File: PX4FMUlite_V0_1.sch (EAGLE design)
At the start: 192 parts, among them J201 DF13C-6P-1.25V, J202 DF13C-6P-1.25V, J203 DF13C-6P-1.25V, J204 DF13C-6P-1.25V, J301 47346-0001, J302 DF13C-4P-1.25V, J401 DF13C-4P-1.25V, J403 DF13C-7P-1.25V, J404 DF13C-5P-1.25V, J405 DF13C-4P-1.25V, J601 DF13C-6P-1.25V, J702 DF13C-3P-1.25V, J801 JST-ZH-3, J901 HEADER-3X163X16RA, M3_MOUNT1101 MOUNT-HOLE3.1MM, M3_MOUNT1102 MOUNT-HOLE3.1MM, M3_MOUNT1103 MOUNT-HOLE3.1MM, M3_MOUNT1104 MOUNT-HOLE3.1MM, U101 STM32F4X7VX, U102 FM25V01, U201 TXS0108QFN20, U202 TXS0108QFN20, U301 2908-05WB-MG, U401 MAX3051, U502 L3GD20H, U503 MS5611-01BA, U701 TCA62724FMG, U703 LRTB GFTG-T7AW-1+V7A7-29+R5T9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, U901 TXS0108QFN20, U903 74LVC2G240, X101 3.2x2.5 mm / 24 MHz / 15 ppm

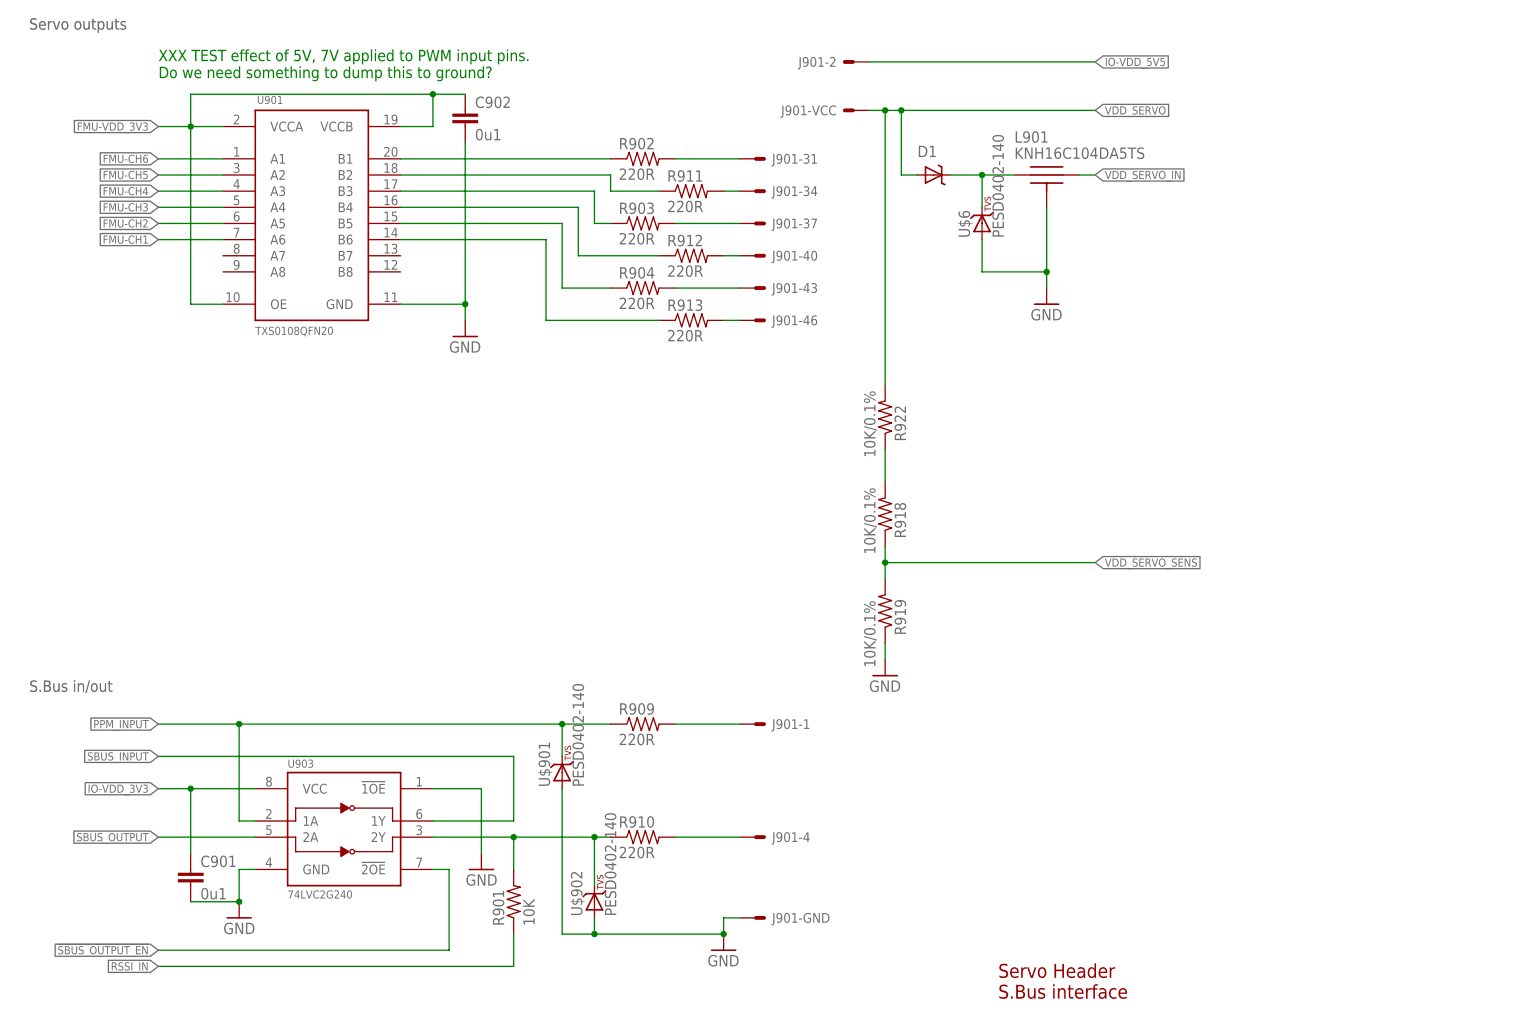
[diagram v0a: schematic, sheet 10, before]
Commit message: Resize board, resized servo conn plus more
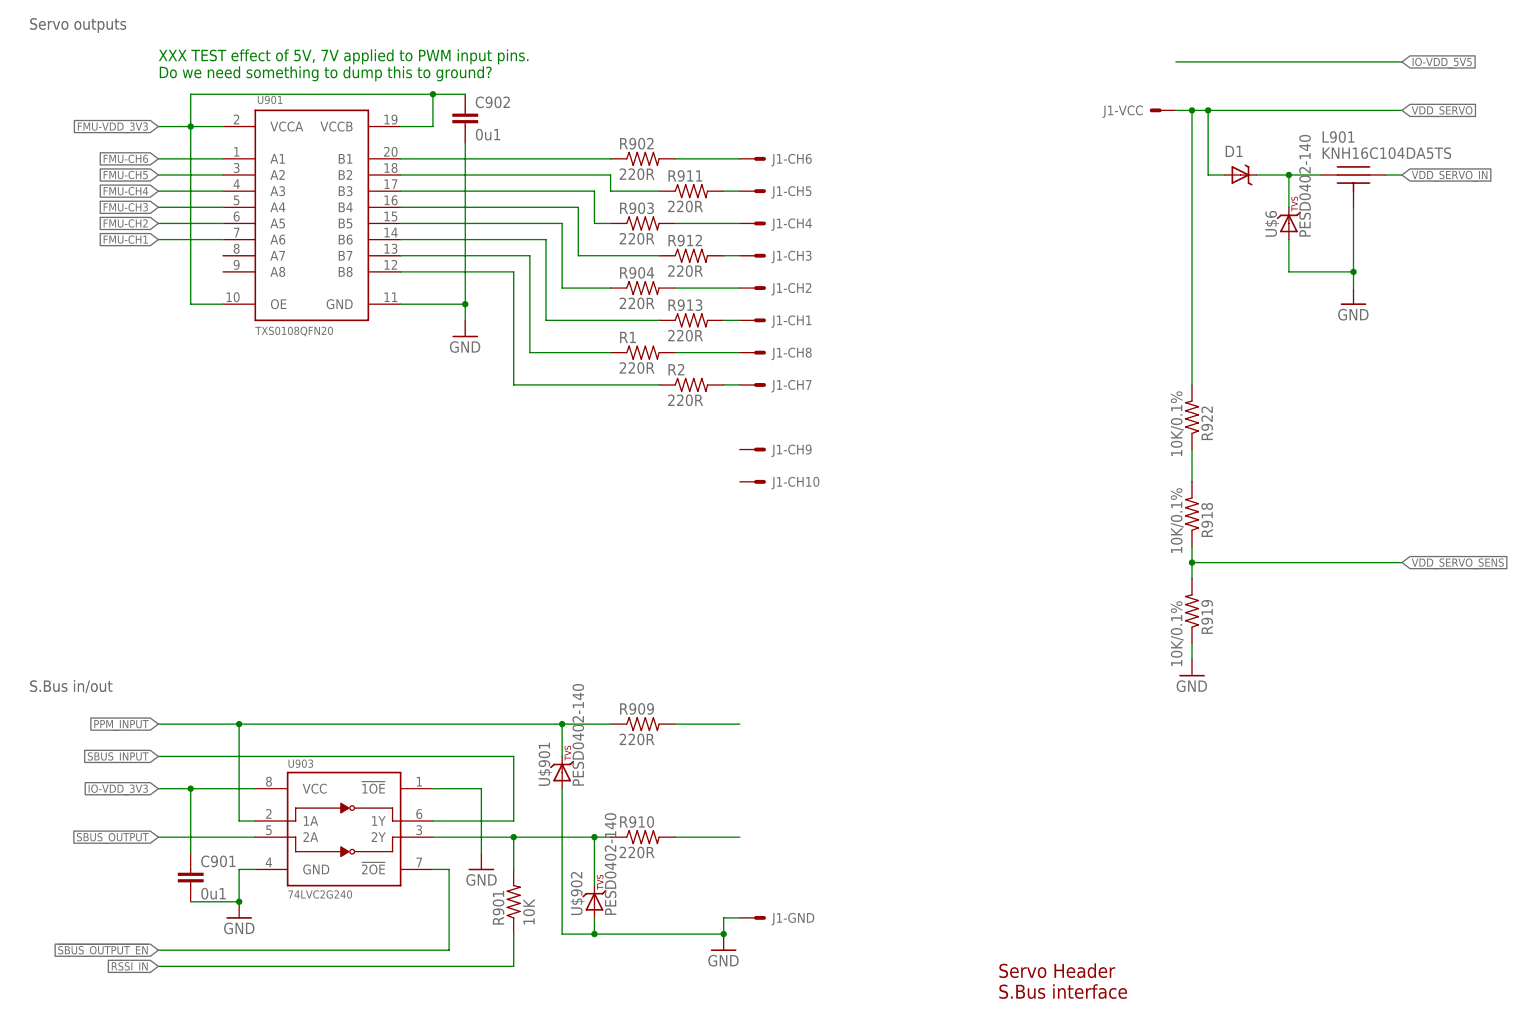
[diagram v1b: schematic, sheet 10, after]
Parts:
- removed J901: HEADER-3X163X16RA, pixhawk2:HEADER-3X163X16RA
- added J1: (no value), PX4lite:HEADER-3X10
- added R1, R2: 220R, pixhawk2:RESISTOR0402-RES
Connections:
- new net N$15: J1-CH8.S, R1.2
- new net N$16: J1-CH7.S, R2.2
- new net N$18: R1.1, U901.B7
- new net N$21: R2.1, U901.B8
- net FMU-CH1-PROT: now also J1-CH1.S; no longer J901-46.S
- net FMU-CH6-PROT: now also J1-CH6.S; no longer J901-31.S
- net GNDX: now also J1-GND.S; no longer J901-GND.S
- net IO-VDD_5V5: no longer J901-2.S
- net N$68: now also J1-CH5.S; no longer J901-34.S
- net N$77: now also J1-CH4.S; no longer J901-37.S
- net N$78: now also J1-CH3.S; no longer J901-40.S
- net N$79: now also J1-CH2.S; no longer J901-43.S
- net N$99: no longer J901-4.S
- net PPM-SBUS-PROT: no longer J901-1.S
- net VDD_SERVO: now also J1-VCC.S; no longer J901-VCC.S
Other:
- moved on the sheet: D1, L901, R918, R919, R922, U$6

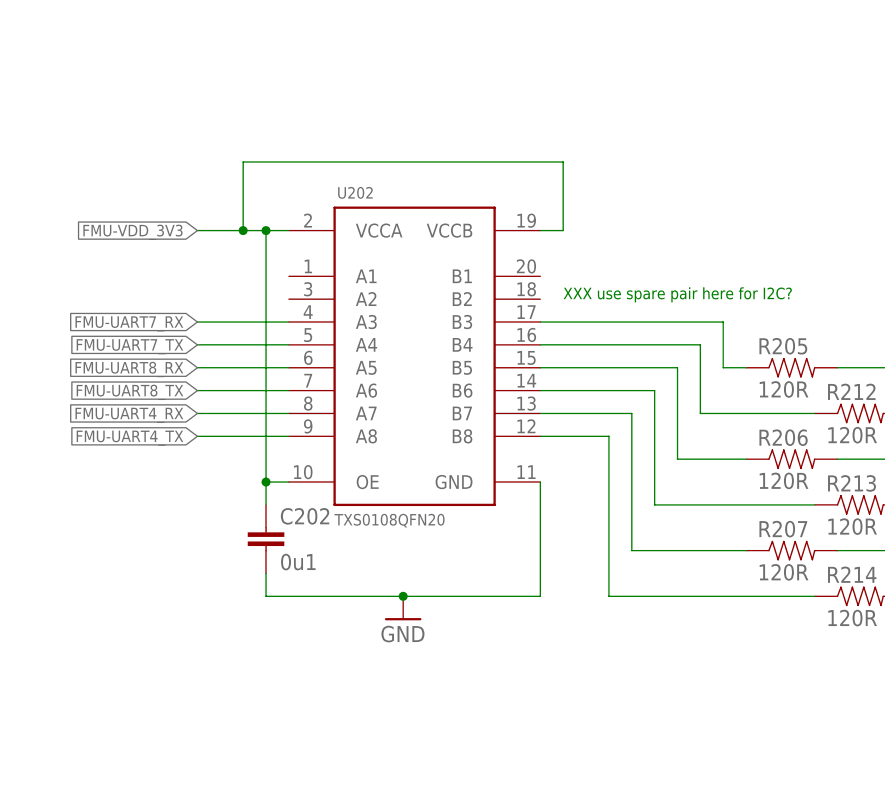
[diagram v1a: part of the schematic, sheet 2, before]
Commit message: Removed TXS0105 buffer on excess uarts
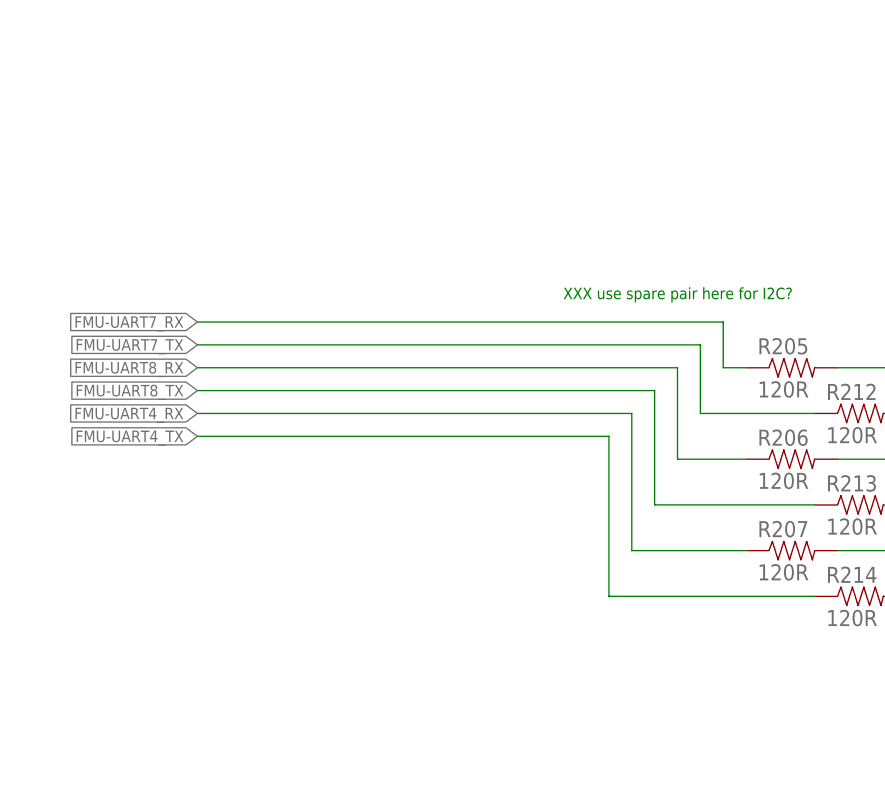
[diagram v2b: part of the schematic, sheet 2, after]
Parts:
- removed C202: 0u1, pixhawk2:CAP0402
- removed U202: TXS0108QFN20, pixhawk2:TXS0108QFN20
- removed U503: MS5611-01BA, pixhawk2:MS5611-01BA
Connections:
- removed net N$90: R214.1, U202.B8
- removed net N$91: R205.1, U202.B3
- removed net N$92: R212.1, U202.B4
- removed net N$93: R206.1, U202.B5
- removed net N$94: R213.1, U202.B6
- net !BARO_CS: no longer U503.CSB2
- net FMU-UART4_RX: no longer U202.A7
- net FMU-UART4_TX: now also R214.1; no longer U202.A8
- net FMU-UART7_RX: now also R205.1; no longer U202.A3
- net FMU-UART7_TX: now also R212.1; no longer U202.A4
- net FMU-UART8_RX: now also R206.1; no longer U202.A5
- net FMU-UART8_TX: now also R213.1; no longer U202.A6
- net FMU-VDD_3V3: no longer C202.1, U202.OE, U202.VCCA, U202.VCCB
- net GNDX: no longer C202.2, U202.GND, U503.GND, U503.PS
- net N$89: no longer U202.B7
- net SPI_INT_MISO: no longer U503.SDO
- net SPI_INT_MOSI: no longer U503.SDI/SDA
- net SPI_INT_SCK: no longer U503.SCLK
- net VDD_3V3_SENSORS: no longer U503.VDD

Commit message: Replaced lvl translators with NFU8042 ESD/EMI filters
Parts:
- removed C201, C902: 0u1, pixhawk2:CAP0402
- removed R1, R2, R902, R903, R904, R911, R912, R913: 220R, pixhawk2:RESISTOR0402-RES
- removed R201, R202, R203, R204, R205, R206, R207, R208, R209, R210, R211, R212, R213, R214: 120R, pixhawk2:RESISTOR0402-RES
- removed U201, U901: TXS0108QFN20, pixhawk2:TXS0108QFN20
- added L1, L2, L3: NUF8402MN, PX4lite:NUF8402MN
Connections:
- removed net FMU-CH6-PROT: J1-CH6.S, R902.2
- removed net N$18: R1.1, U901.B7
- removed net N$21: R2.1, U901.B8
- removed net N$61: R902.1, U901.B1
- removed net N$62: R911.1, U901.B2
- removed net N$63: R903.1, U901.B3
- removed net N$64: R912.1, U901.B4
- removed net N$65: R904.1, U901.B5
- removed net N$66: R913.1, U901.B6
- removed net N$70: R201.1, U201.B1
- removed net N$82: R208.1, U201.B2
- removed net N$83: R202.1, U201.B3
- removed net N$84: R209.1, U201.B4
- removed net N$85: R203.1, U201.B5
- removed net N$86: R210.1, U201.B6
- removed net N$87: R204.1, U201.B7
- removed net N$88: R211.1, U201.B8
- removed net N$89: R207.1
- new net N$32: L1G$7.P$1
- new net N$36: J1-CH6.S, L1G$6.P$2
- net FMU-CH1: no longer U901.A6
- net FMU-CH1-PROT: now also L1G$1.P$2; no longer R913.2
- net FMU-CH2: no longer U901.A5
- net FMU-CH3: no longer U901.A4
- net FMU-CH4: no longer U901.A3
- net FMU-CH5: no longer U901.A2
- net FMU-CH6: no longer U901.A1
- net FMU-UART4_RX: now also L3G$5.P$1
- net FMU-UART4_TX: now also L3G$6.P$1; no longer R214.1
- net FMU-UART7_RX: now also L3G$1.P$1; no longer R205.1
- net FMU-UART7_TX: now also L3G$2.P$1; no longer R212.1
- net FMU-UART8_RX: now also L3G$3.P$1; no longer R206.1
- net FMU-UART8_TX: now also L3G$4.P$1; no longer R213.1
- net FMU-USART2_CTS: now also L2G$8.P$1; no longer U201.A8
- net FMU-USART2_RTS: now also L2G$7.P$1; no longer U201.A7
- net FMU-USART2_RX: now also L2G$5.P$1; no longer U201.A5
- net FMU-USART2_TX: now also L2G$6.P$1; no longer U201.A6
- net FMU-USART3_CTS: now also L2G$2.P$1; no longer U201.A2
- net FMU-USART3_RTS: now also L2G$1.P$1; no longer U201.A1
- net FMU-USART3_RX: now also L2G$3.P$1; no longer U201.A3
- net FMU-USART3_TX: now also L2G$4.P$1; no longer U201.A4
- net FMU-VDD_3V3: no longer C201.1, C902.1, U201.OE, U201.VCCA, U201.VCCB, U901.OE, U901.VCCA, U901.VCCB
- net GNDX: no longer C201.2, C902.2, U201.GND, U901.GND
- net N$15: now also L1G$8.P$2; no longer R1.2
- net N$16: no longer R2.2
- net N$68: no longer R911.2
- net N$77: now also L1G$4.P$2; no longer R903.2
- net N$78: now also L1G$3.P$2; no longer R912.2
- net N$79: now also L1G$2.P$2; no longer R904.2
- net SERIAL1_CTS: now also L2G$8.P$2; no longer R211.2
- net SERIAL1_RTS: now also L2G$7.P$2; no longer R204.2
- net SERIAL1_RX: now also L2G$5.P$2; no longer R203.2
- net SERIAL1_TX: now also L2G$6.P$2; no longer R210.2
- net SERIAL2_CTS: now also L2G$2.P$2; no longer R208.2
- net SERIAL2_RTS: now also L2G$1.P$2; no longer R201.2
- net SERIAL2_RX: now also L2G$3.P$2; no longer R202.2
- net SERIAL2_TX: now also L2G$4.P$2; no longer R209.2
- net SERIAL3_RX: now also L3G$5.P$2; no longer R207.2
- net SERIAL3_TX: now also L3G$6.P$2; no longer R214.2
- net SERIAL4_RX: now also L3G$3.P$2; no longer R206.2
- net SERIAL4_TX: now also L3G$4.P$2; no longer R213.2
- net SERIAL5_RX: now also L3G$1.P$2; no longer R205.2
- net SERIAL5_TX: now also L3G$2.P$2; no longer R212.2
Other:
- note removed: "XXX TEST effect of 5V, 7V applied to PWM input pins. Do we need something to dump this to ground?"
- note removed: "XXX use spare pair here for I2C?"
